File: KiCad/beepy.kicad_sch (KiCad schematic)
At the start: 102 parts, among them J1 FDX0019B1, J10 FDX0019B1, J11 FDX0019B1, J12 FDX0019B1, J13 FDX0019B1, J14 FDX0019B1, J15 USB_C_Receptacle_USB2.0, J16 FDX0019B1, J17 FDX0019B1, J18 FDX0019B1, J19 FDX0019B1, J2 FDX0019B1, J20 FDX0019B1, J21 FDX0019B1, J22 Pi Zero, J23 FDX0019B1, J24 FDX0019B1, J25 FDX0019B1, J26 FDX0019B1, J27 FDX0019B1, J28 FDX0019B1, J29 FDX0019B1, J3 FDX0019B1, J30 FDX0019B1, J31 FDX0019B1, J32 FDX0019B1, J33 FDX0019B1, J34 FDX0019B1, J35 FDX0019B1, J36 FDX0019B1, J37 FDX0019B1, J38 FDX0019B1, J39 FDX0019B1, J4 FDX0019B1, J40 FDX0019B1, J41 FDX0019B1, J42 FDX0019B1, J43 Battery, J44 Header 1, J45 PRG_HEADER, J46 Header 2, J47 Header 3, J5 FDX0019B1, J6 FDX0019B1, J7 FDX0019B1, J8 FDX0019B1, J9 FDX0019B1, Q1 SI2301, Q2 SI2301, Q9 S8050, SW1 ON/OFF, SW2 Button, U1 TP4054, U2 TPS61090, U3 LS027B7DH01

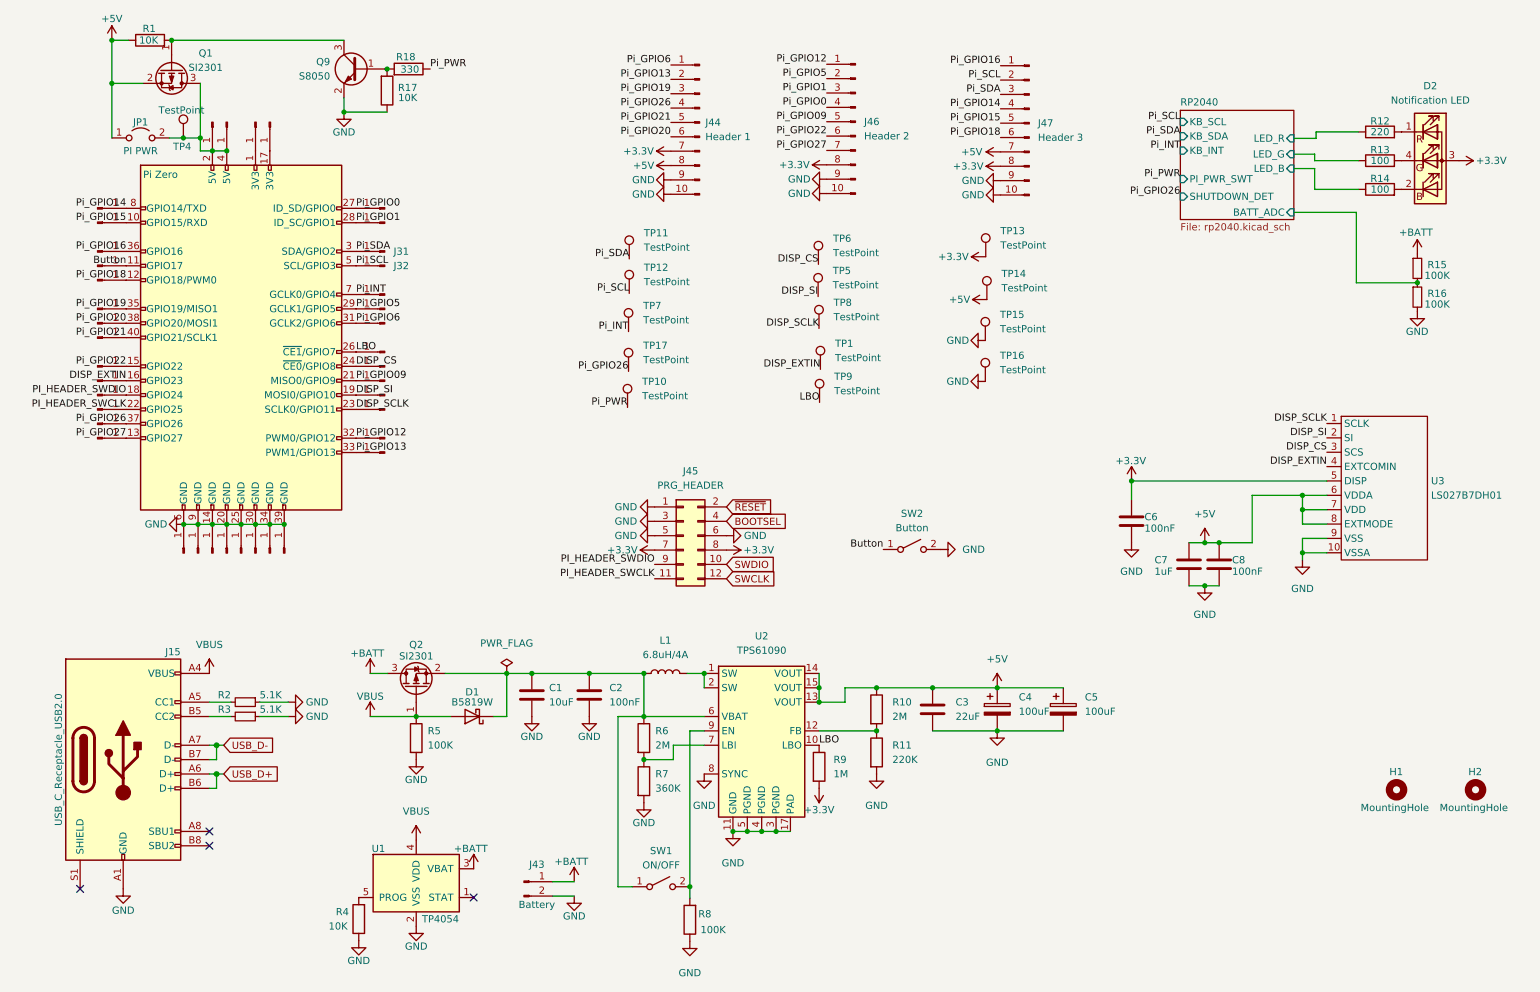
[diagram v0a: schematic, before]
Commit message: Importing to KiCAD 8 and using pin headers instead of springs
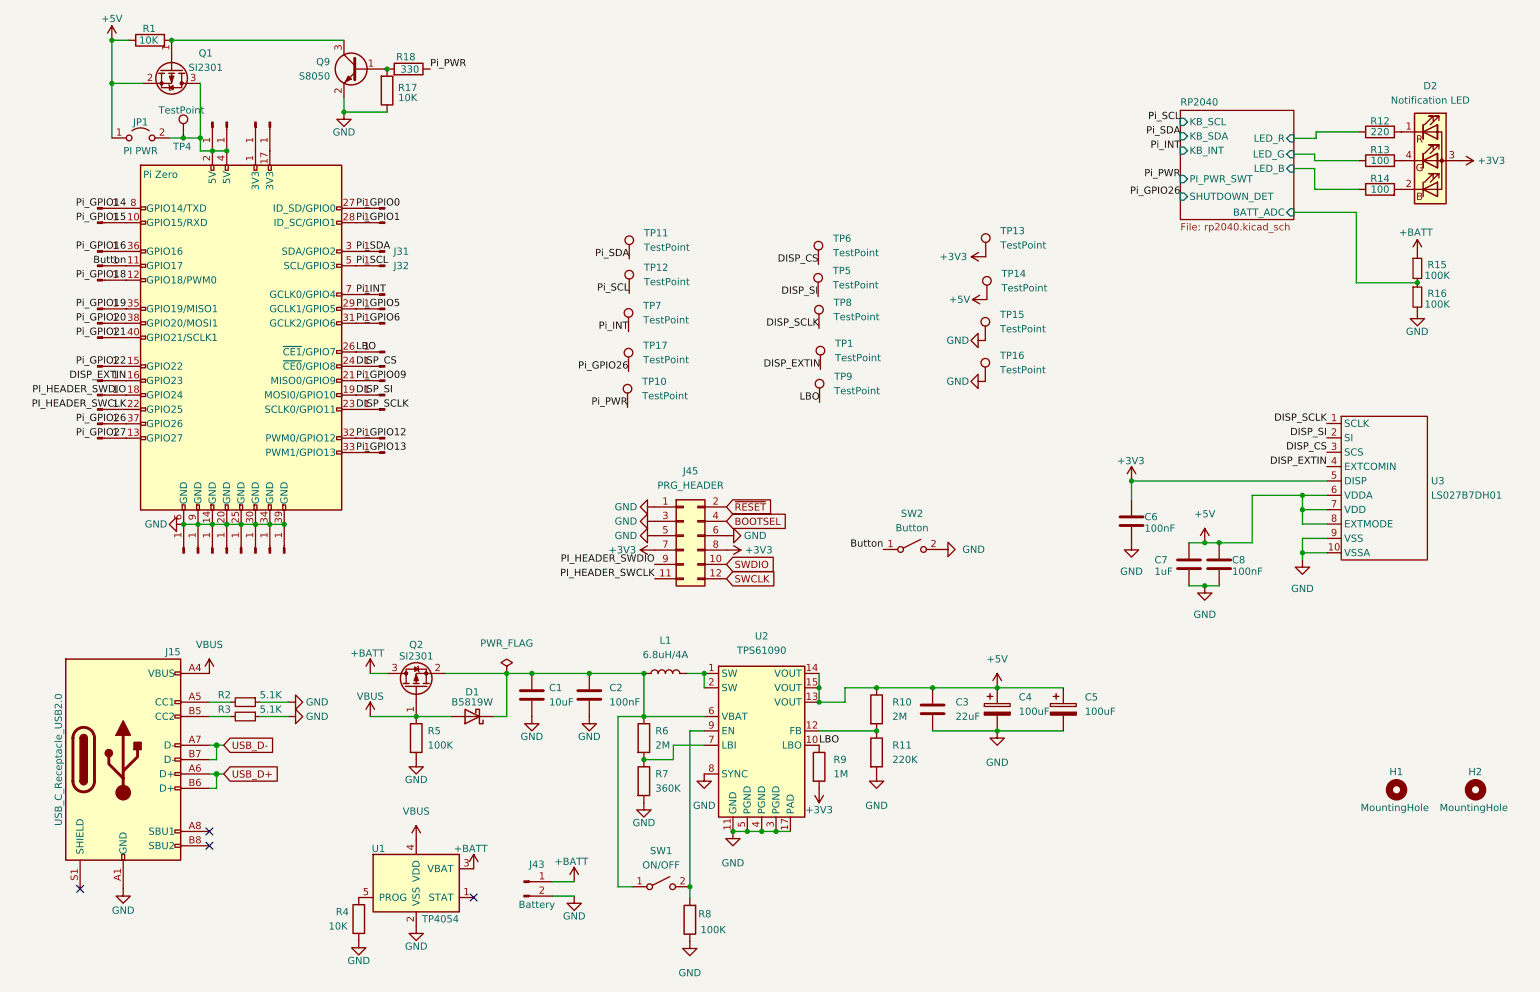
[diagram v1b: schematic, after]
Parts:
- removed J44: Header 1, Connector_PinHeader_2.54mm:PinHeader_1x10_P2.54mm_Vertical, symbol Connector:Conn_01x10_Male
- removed J46: Header 2, Connector_PinHeader_2.54mm:PinHeader_1x10_P2.54mm_Vertical, symbol Connector:Conn_01x10_Male
- removed J47: Header 3, Connector_PinHeader_2.54mm:PinHeader_1x10_P2.54mm_Vertical, symbol Connector:Conn_01x10_Male
- J22: footprint beepy:Raspberry_Pi_Zero_Socketed_SMD_FaceUP_MountingHoles -> Connector_PinHeader_2.54mm:PinHeader_2x20_P2.54mm_Vertical_SMD
